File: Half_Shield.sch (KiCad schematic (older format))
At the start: 43 parts, among them U1 TPS561208DDC

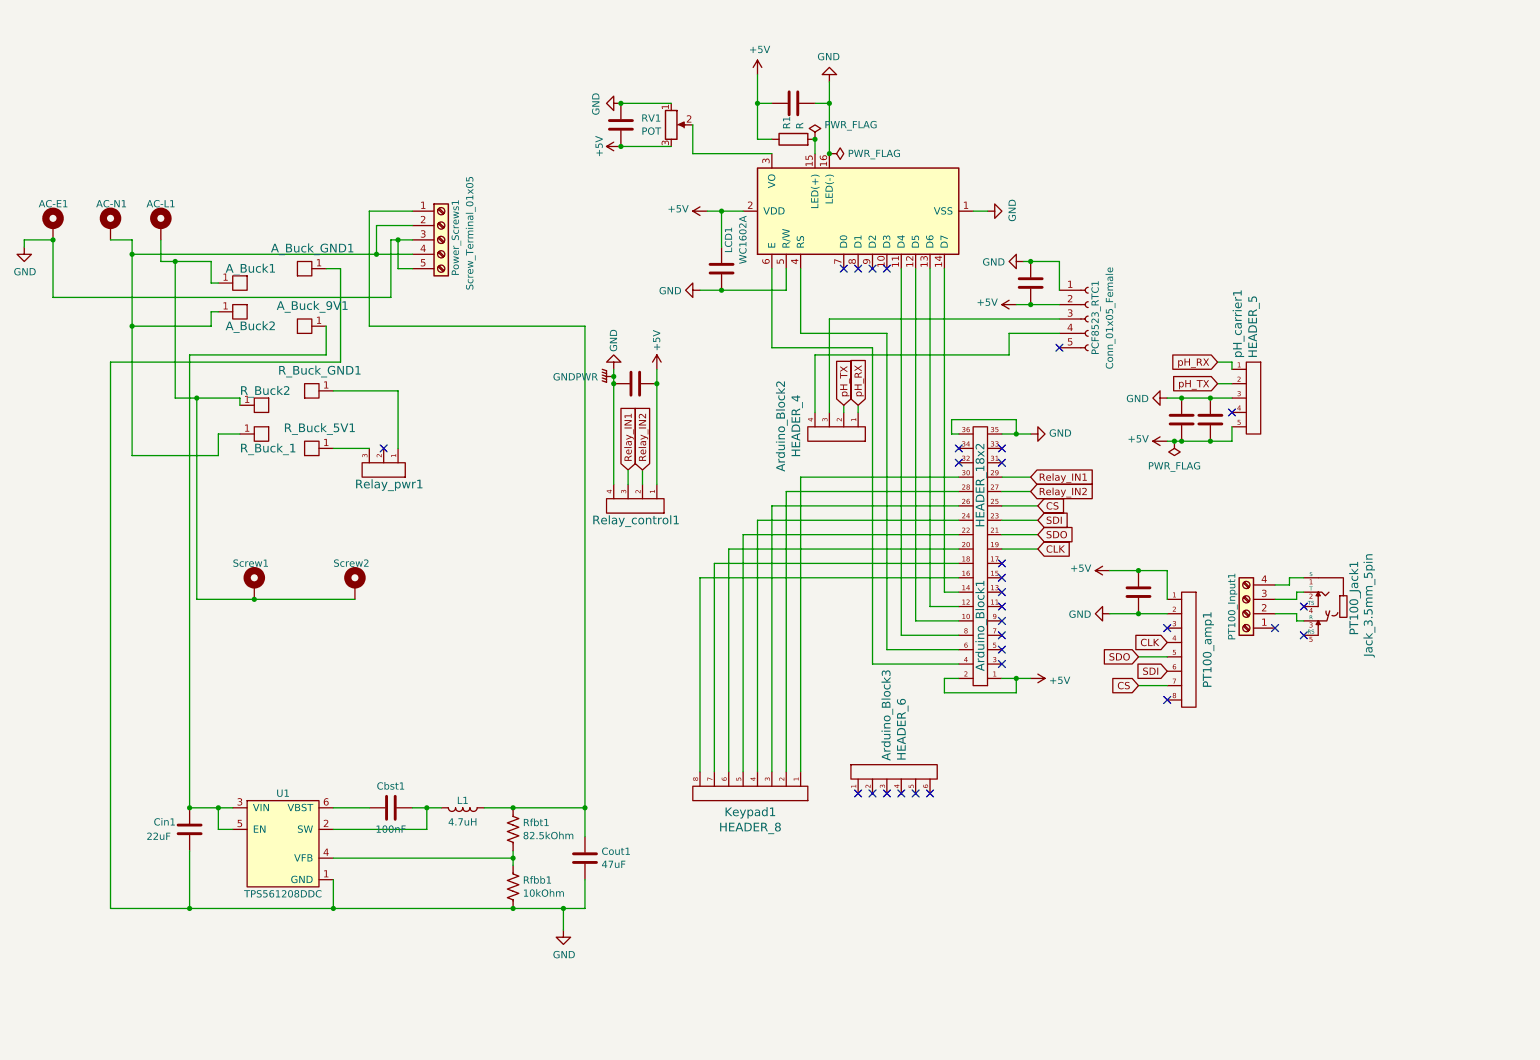
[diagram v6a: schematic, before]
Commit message: added jumpers for alternate power
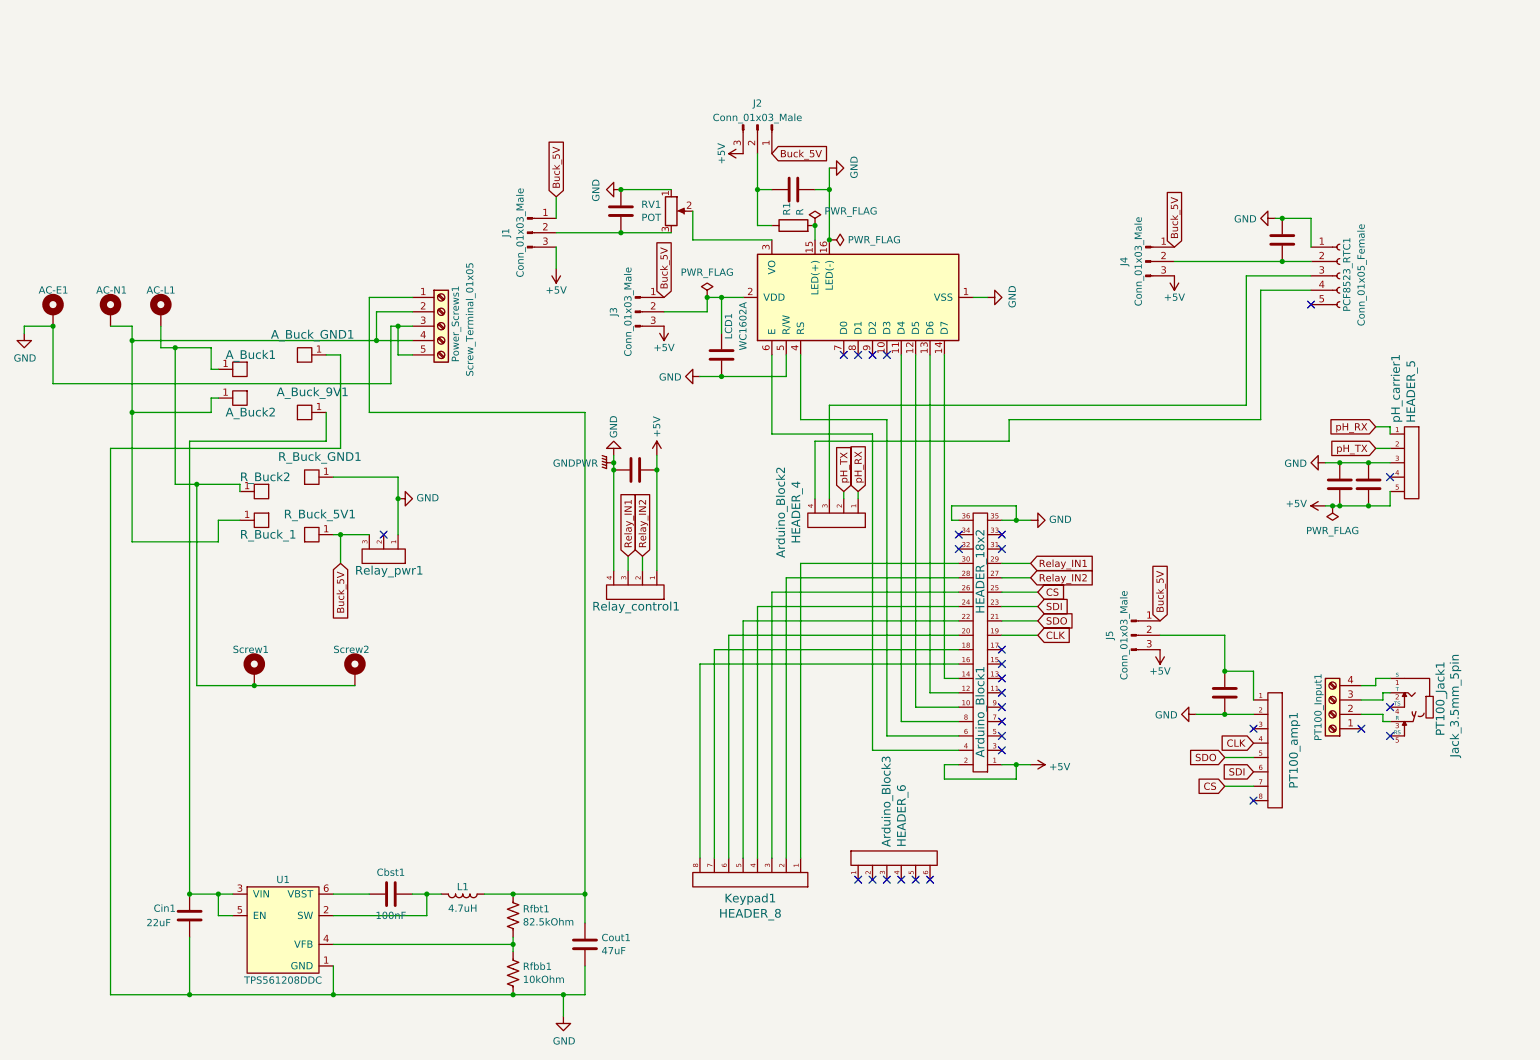
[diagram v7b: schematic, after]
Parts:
- added J1, J2, J3, J4, J5: Conn_01x03_Male, Pin_Headers:Pin_Header_Straight_1x03_Pitch2.54mm, symbol Connector:Conn_01x03_Male
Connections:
- net +5V: now also J1.3 (Pin_3), J2.3 (Pin_3), J3.3 (Pin_3), J4.3 (Pin_3), J5.3 (Pin_3); no longer C2.2, C3.2, C4.1, C5.2, C8.2, LCD1.2 (VDD), PCF8523_RTC1.2 (Pin_2), PT100_amp1.1, R1.1, RV1.3
- net GND: now also R_Buck_GND1.1, Relay_pwr1.1
- net Buck_5V: now reaches R_Buck_5V1.1, Relay_pwr1.3
- net Buck_5V: now also J1.1 (Pin_1), J2.1 (Pin_1), J3.1 (Pin_1), J4.1 (Pin_1), J5.1 (Pin_1)
- new net: C2.2, J3.2 (Pin_2), LCD1.2 (VDD)
- new net: C4.1, J2.2 (Pin_2), R1.1
- new net: C3.2, J1.2 (Pin_2), RV1.3
- new net: C5.2, J5.2 (Pin_2), PT100_amp1.1
- new net: C8.2, J4.2 (Pin_2), PCF8523_RTC1.2 (Pin_2)
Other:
- moved on the sheet: AC-E1, AC-L1, AC-N1, A_Buck1, A_Buck2, A_Buck_9V1, A_Buck_GND1, Arduino_Block1, Arduino_Block2, Arduino_Block3, Cbst1, Cin1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
